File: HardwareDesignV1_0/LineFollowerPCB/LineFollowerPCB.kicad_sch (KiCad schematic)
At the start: 11 parts, among them J1 B2B-XH-A, J2 B4B-XH-A, J3 Conn_01x04, M1 Motor_DC, M2 Motor_DC, U1 Black Pill v2, U2 DRV8833, U3 AMS1117-3.3, U4 SX1308

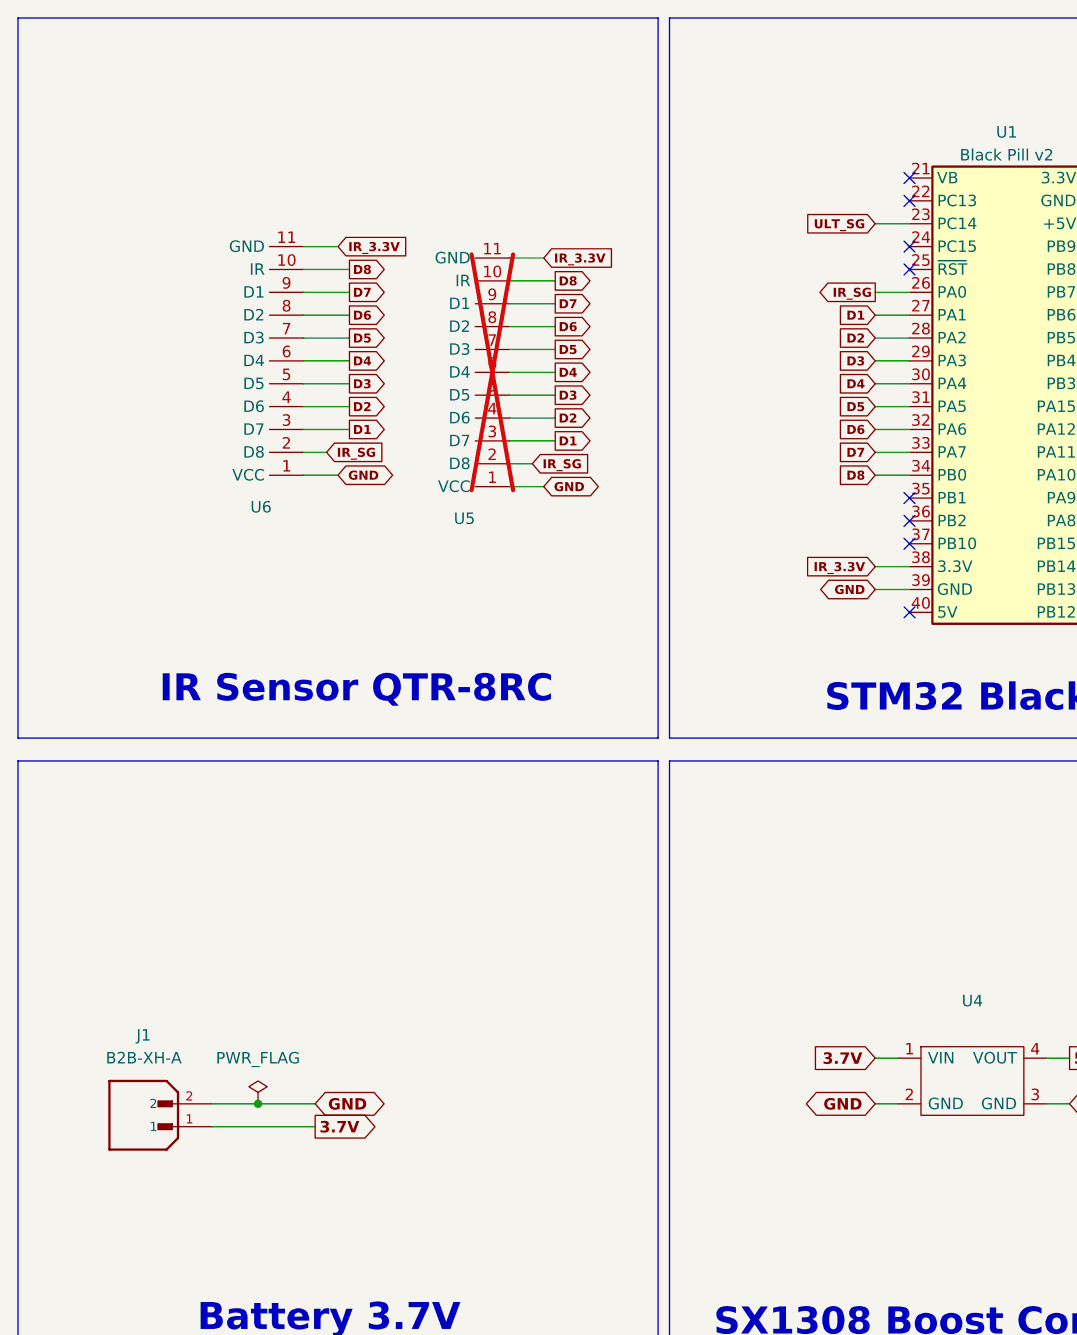
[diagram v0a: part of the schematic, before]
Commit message: - Add Shunt bridge for power switching ON-OFF - Edit DC motor footprint library - Add solder jumber for select between QTR / Cytron sensors
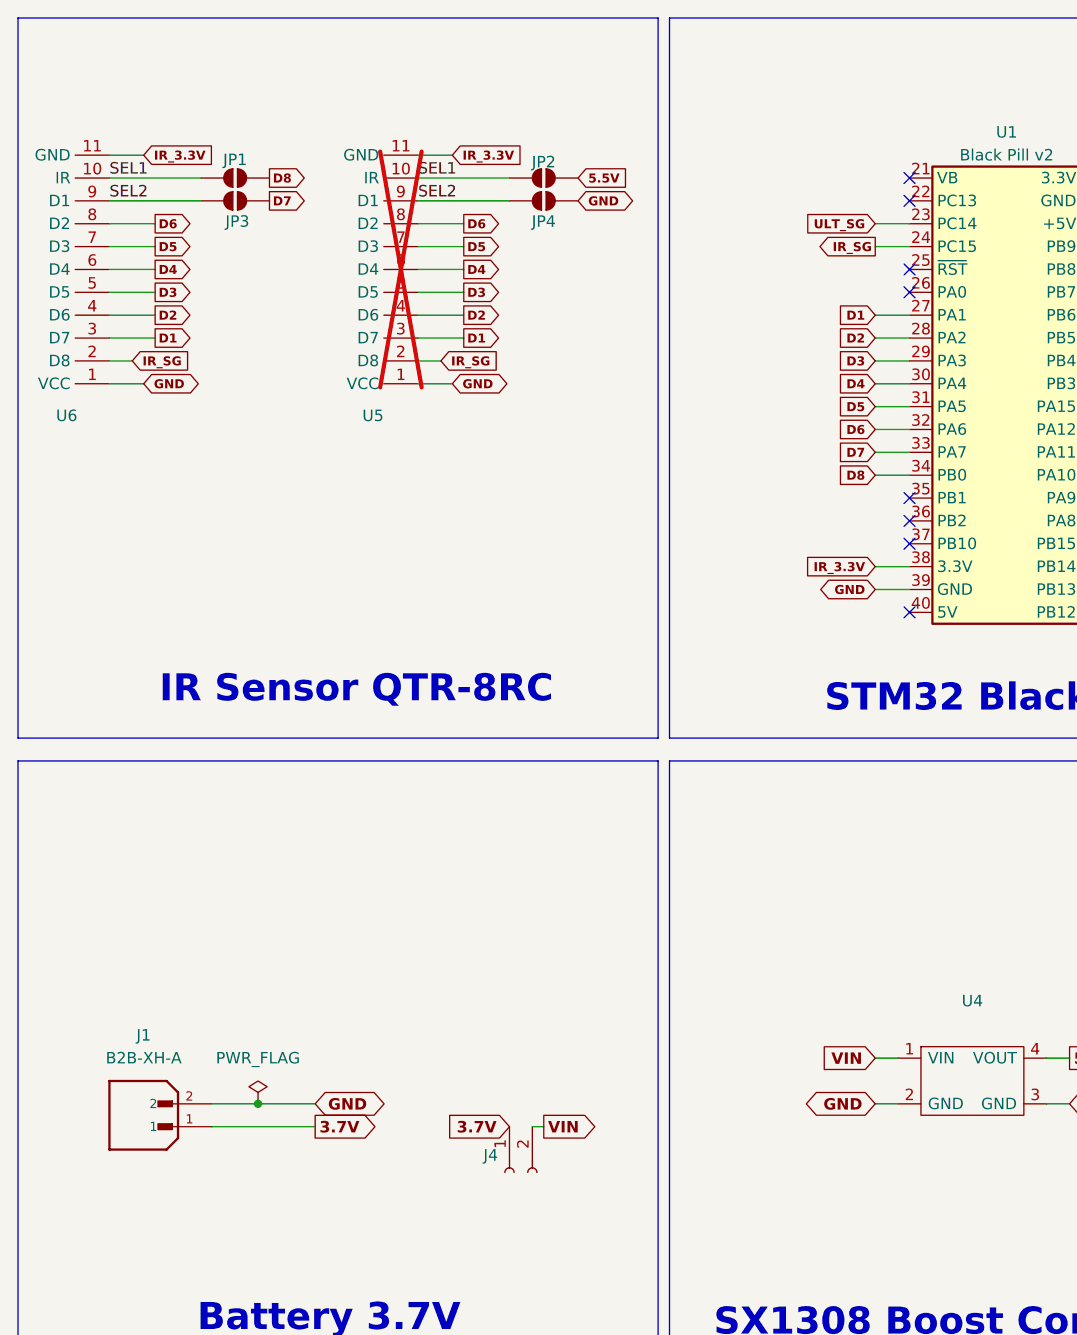
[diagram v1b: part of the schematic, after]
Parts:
- added J4: Conn_01x02_Socket, Connector_PinHeader_2.54mm:PinHeader_1x02_P2.54mm_Vertical, symbol Connector:Conn_01x02_Socket
- added JP1, JP2, JP3, JP4: SolderJumper_3_Open, Jumper:SolderJumper-2_P1.3mm_Open_RoundedPad1.0x1.5mm, symbol Jumper:SolderJumper_2_Open
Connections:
- net 3.7V: now also J4.1 (Pin_1); no longer U4.1 (VIN)
- net 5.5V: now also JP2.1 (A)
- net D7: now also JP3.1 (A); no longer U5.9 (D1), U6.9 (D1)
- net D8: now also JP1.2 (B); no longer U5.10 (IR), U6.10 (IR)
- net GND: now also JP4.2 (B)
- net IR_SG: now also U1.24 (PC15); no longer U1.26 (PA0)
- new net SEL1: JP1.1 (A), JP2.2 (B), U5.10 (IR), U6.10 (IR)
- new net SEL2: JP3.2 (B), JP4.1 (A), U5.9 (D1), U6.9 (D1)
- new net VIN: J4.2 (Pin_2), U4.1 (VIN)
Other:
- moved on the sheet: U5, U6
